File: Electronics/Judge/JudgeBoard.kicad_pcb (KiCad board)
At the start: 2 copper layers, 124.2 x 71.1 mm, 29 parts, among them J1 RJ12-UNSHLD, U1 74HC165, U2 74HC165, U3 MIC5504-3.3YM5

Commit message: Intermediate commit while moving components to final locations.
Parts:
- added C5: 470pF, Capacitor_SMD:C_1206_3216Metric_Pad1.42x1.75mm_HandSolder, F.Cu at (152.1, 65.7)
- added C6: 470pF, Capacitor_SMD:C_1206_3216Metric_Pad1.42x1.75mm_HandSolder, F.Cu at (148.6, 65.7)
- J1: value RJ12-UNSHLD -> RJ10; footprint PiKwonDo:TH-RJ12 -> Local_lib:RJ14
- moved R4 11.4 mm to (142.1, 93.2), turned to 0 degrees
- moved D5 9.43 mm to (136.1, 98.2)
- moved J1 9.41 mm to (154.1, 115.2), turned to 180 degrees
- moved C3 8.52 mm to (132.1, 98.2)
- moved C4 8.51 mm to (163.4, 90.2)
- moved D3 8.51 mm to (168.8, 90.2)
- moved D2 7.77 mm to (134.6, 93.2)
- moved RN2 7.25 mm to (171.6, 81.2)
- moved U3 6.73 mm to (131.6, 88.7), turned to 90 degrees
- moved C1 6.03 mm to (131.9, 84.7)
- moved R2 5.70 mm to (161.6, 86.2)
- moved U2 5.49 mm to (158.1, 83.7)
- moved C2 5.20 mm to (168.6, 82.7)
- moved U1 4.30 mm to (144.6, 65.8)
- moved RN1 4.17 mm to (132.1, 81.1)
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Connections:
- net /Q_intermediate renamed /Q_inter
- J1 pad 1: Net-(J1-Pad1) -> GND
- J1 pad 2: Net-(J1-Pad2) -> Net-(C4-Pad1)
- J1 pad 4: Net-(C4-Pad1) -> Net-(J1-Pad4)
- R1 pad 2: Net-(J1-Pad2) -> Net-(J1-Pad4)
- R4 pad 2: Net-(J1-Pad2) -> Net-(J1-Pad4)
- R5 pad 2: Net-(J1-Pad2) -> Net-(J1-Pad4)
- U2 pad 11: Net-(RN2-Pad6) -> Net-(RN2-Pad5)
- U2 pad 12: Net-(RN2-Pad5) -> Net-(RN2-Pad4)
- U2 pad 13: Net-(RN2-Pad4) -> Net-(RN2-Pad3)
- U2 pad 14: Net-(RN2-Pad3) -> Net-(RN2-Pad2)
- U2 pad 3: Net-(RN2-Pad2) -> GND
- U2 pad 6: GND -> Net-(RN2-Pad6)
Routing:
- net GND: track 573.7 -> 46.7 mm, vias 0 -> 4
- net Net-(RN1-Pad5): track 40.2 -> 3.41 mm
- net Net-(RN2-Pad2): track 45.6 -> 12.4 mm
- net Net-(RN2-Pad6): track 36.2 -> 3.01 mm
- net +3V3: track 74.6 -> 106.9 mm, vias 0 -> 2
- net /LOAD: track 40.2 -> 13.1 mm
- net /CLK: track 32.1 -> 6.06 mm
- net Net-(RN2-Pad4): track 52.5 -> 27.4 mm
- net Net-(RN2-Pad3): track 37.5 -> 13.0 mm
- net Net-(RN1-Pad3): track 31.7 -> 7.74 mm
- net Net-(J1-Pad2): track 22.4 -> 0.00 mm
- net +5V: track 22.2 -> 0.00 mm
- net Net-(RN2-Pad5): track 21.3 -> 3.30 mm
- net Net-(RN1-Pad2): track 38.2 -> 24.0 mm
- net /Q: track 14.0 -> 0.00 mm
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- added copper zone on F.Cu, net GND
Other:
- board size 124.2 x 71.1 mm -> 124.2 x 71.8 mm
- net class Default: clearance 0.3 -> 0.31; trace_width 0.4 -> 0.5
- rule trace_clearance: 0.3 -> 0.31

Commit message: Finalized trace routing and part placement.
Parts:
- moved R3 24.7 mm to (158.4, 89.4), turned to 90 degrees
- moved D1 17.4 mm to (153.6, 91.7), turned to 180 degrees
- moved J1 16.7 mm to (156.6, 98.7)
- moved R1 9.01 mm to (147.1, 93.2), turned to 270 degrees
- moved R5 6.95 mm to (144.1, 93.2), turned to 270 degrees
- moved C4 3.25 mm to (163.4, 93.4)
- moved D3 3.25 mm to (168.8, 93.4)
- moved R2 2.37 mm to (162.4, 88.4)
- moved R4 1.00 mm to (141.1, 93.2), turned to 270 degrees
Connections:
- S10 pad 1: Net-(RN2-Pad5) -> Net-(RN2-Pad4)
- S5 pad 1: Net-(RN2-Pad4) -> Net-(RN2-Pad5)
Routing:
- net /CLK: track 6.06 -> 58.2 mm
- net /Q_inter: track 3.05 -> 53.6 mm, vias 0 -> 2
- net Net-(RN2-Pad5): track 3.30 -> 45.4 mm
- net Net-(RN1-Pad5): track 3.41 -> 39.1 mm
- net Net-(RN2-Pad6): track 3.01 -> 36.2 mm
- net Net-(RN1-Pad6): track 12.2 -> 43.7 mm
- net +3V3: track 106.9 -> 134.9 mm, vias 2 -> 0
- net Net-(RN2-Pad2): track 12.4 -> 37.4 mm
- net /Q: track 0.00 -> 23.2 mm
- net Net-(RN1-Pad3): track 7.74 -> 30.6 mm
- net /LOAD: track 13.1 -> 35.8 mm
- net Net-(RN2-Pad3): track 13.0 -> 33.8 mm
- net Net-(J1-Pad3): track 7.84 -> 28.4 mm
- net Net-(RN1-Pad2): track 24.0 -> 40.5 mm
- net +5V: track 0.00 -> 15.6 mm
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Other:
- board size 124.2 x 71.8 mm -> 124.2 x 58.8 mm

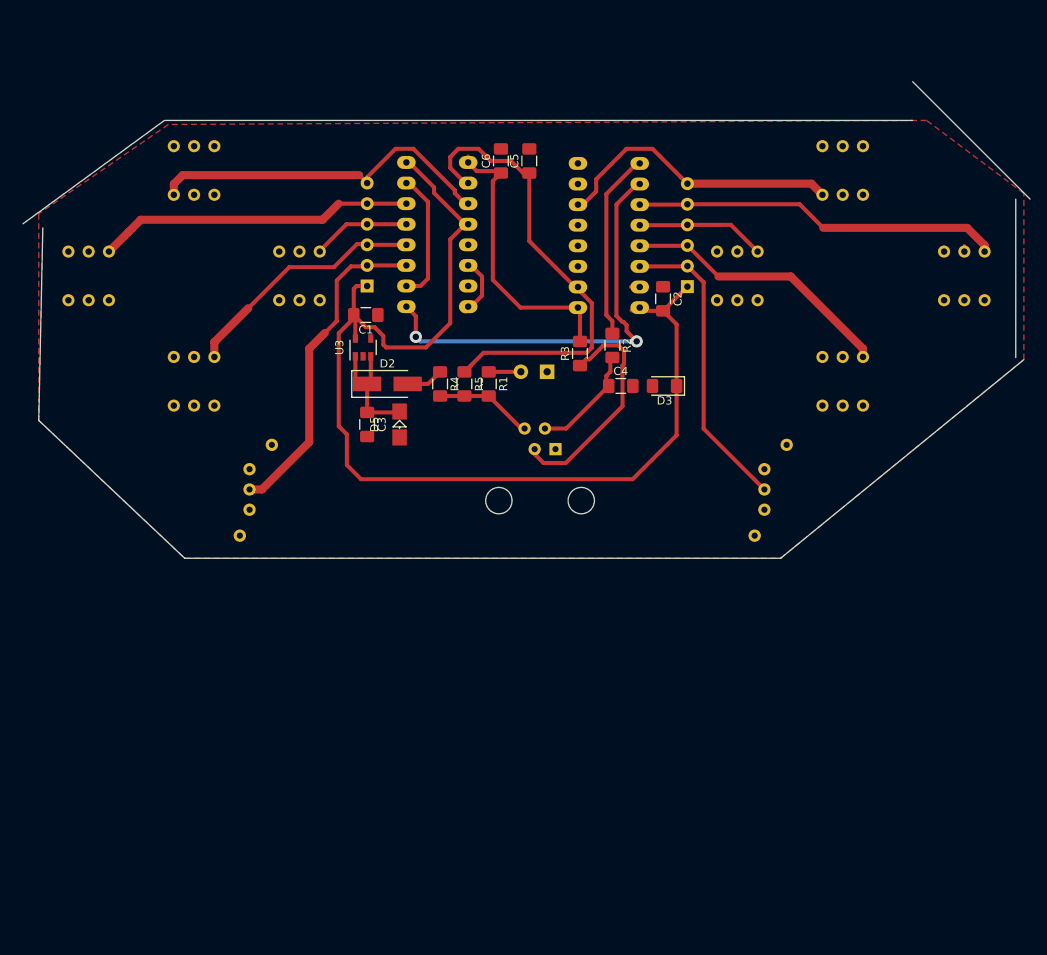
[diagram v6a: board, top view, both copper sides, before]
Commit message: Updated trace routing and board outline. Added mounting holes.
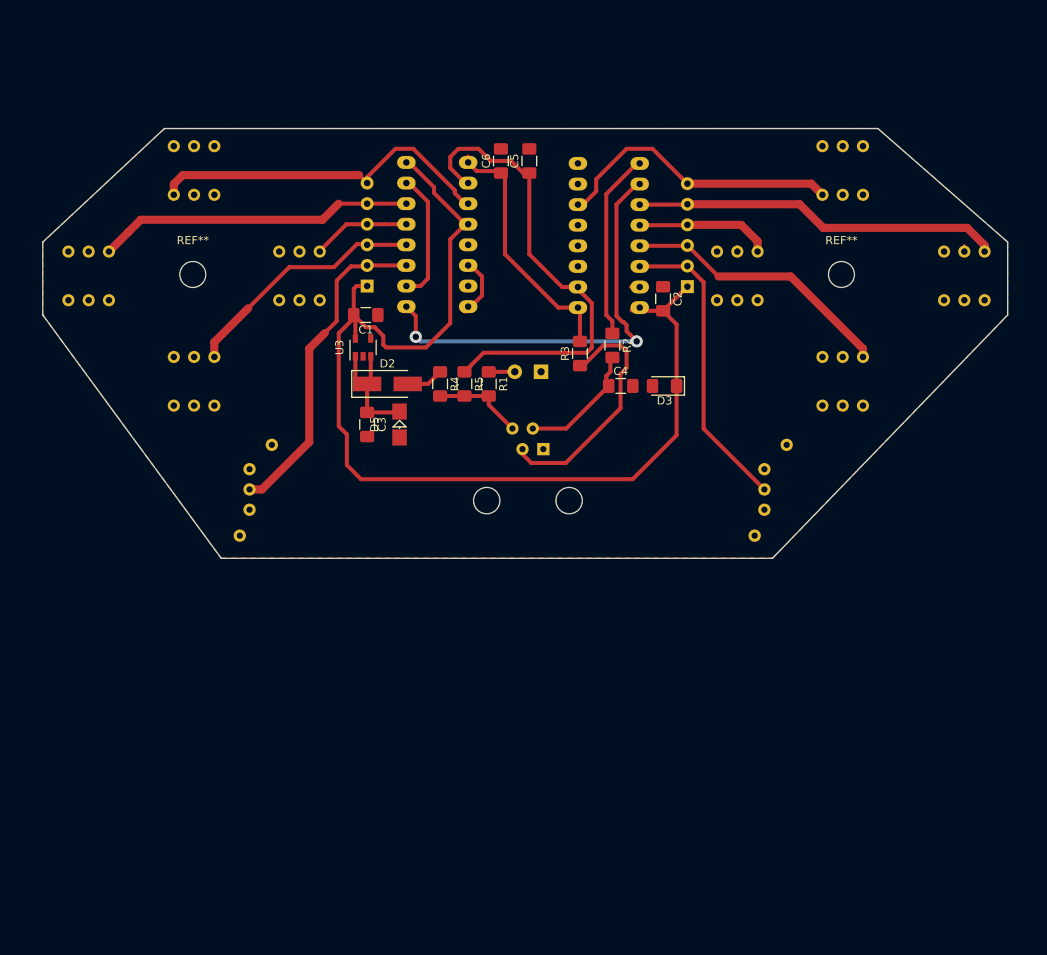
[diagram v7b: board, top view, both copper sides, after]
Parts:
- added REF**: MountingHole_3.2mm_M3, MountingHole:MountingHole_3.2mm_M3, F.Cu at (190.6, 79.7)
- added REF**: MountingHole_3.2mm_M3, MountingHole:MountingHole_3.2mm_M3, F.Cu at (110.6, 79.7)
- moved J1 1.50 mm to (155.1, 98.7)
- moved D1 0.75 mm to (152.9, 91.7)
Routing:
- net /LOAD: track 35.8 -> 32.3 mm
- net Net-(J1-Pad3): track 28.4 -> 30.4 mm
- net Net-(C4-Pad1): track 14.0 -> 15.5 mm
- net /CLK: track 58.2 -> 59.2 mm
- net Net-(J1-Pad4): track 12.1 -> 11.2 mm
- net Net-(D1-Pad2): track 3.97 -> 3.21 mm
- net Net-(RN2-Pad4): track 15.9 -> 16.7 mm
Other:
- board size 124.2 x 58.8 mm -> 119 x 53 mm

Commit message: Updated boards for two-sided manufacture.
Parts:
- removed REF** (x2): MountingHole_3.2mm_M3, MountingHole:MountingHole_3.2mm_M3
- added M3: MountingHole_3.2mm_M3, MountingHole:MountingHole_3.2mm_M3, F.Cu at (190.7, 79.9)
- added M3: MountingHole_3.2mm_M3, MountingHole:MountingHole_3.2mm_M3, F.Cu at (110.8, 79.9)
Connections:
- S1 pad 3: Net-(S1-Pad3) -> (no net)
- S10 pad 3: Net-(S10-Pad3) -> (no net)
- S2 pad 3: Net-(S2-Pad3) -> (no net)
- S3 pad 3: Net-(S3-Pad3) -> (no net)
- S4 pad 3: Net-(S4-Pad3) -> (no net)
- S5 pad 3: Net-(S5-Pad3) -> (no net)
- S6 pad 3: Net-(S6-Pad3) -> (no net)
- S7 pad 3: Net-(S7-Pad3) -> (no net)
- S8 pad 3: Net-(S8-Pad3) -> (no net)
- S9 pad 3: Net-(S9-Pad3) -> (no net)
- U1 pad 7: Net-(U1-Pad7) -> (no net)
- U2 pad 7: Net-(U2-Pad7) -> (no net)
- U3 pad 4: Net-(U3-Pad4) -> (no net)
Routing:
- net GND: track 32.0 -> 57.6 mm, vias 0 -> 2
- net +3V3: track 134.9 -> 142.9 mm
- net /Q_inter: track 53.6 -> 46.5 mm
- net /CLK: track 59.2 -> 60.2 mm
- net /LOAD: track 32.3 -> 31.5 mm
- net Net-(J1-Pad3): track 30.4 -> 31.1 mm
- added copper zone on B.Cu, net GND
- removed copper zone on F.Cu, net GND
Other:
- board text added: "PiKwonDo Judge Board Version 1.0 David Wright 2020"
